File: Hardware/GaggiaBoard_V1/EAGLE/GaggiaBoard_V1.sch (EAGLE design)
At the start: 84 parts, among them IC1 LD117ADT33TR, J2 Vertical Qwiic Connector, J3 Vertical Qwiic Connector, J4 1X2-3.5MM, J5 1X2-3.5MM, K1 RELAY-SPDT-JZC-11F, K2 RELAY-SPDT-JZC-11F, K3 RELAY-SPDT-JZC-11F, Q1 600mA/40V, Q2 600mA/40V, Q3 600mA/40V, Q4 600mA/40V, Q5 600mA/40V, Q6 600mA/40V, Q7 2N7002D, Q8 600mA/40V, Q9 600mA/40V, U1 BLACKPILL, U2 MAX31855K, U3 MAX31855K, U4 MOC3021MDIL06O

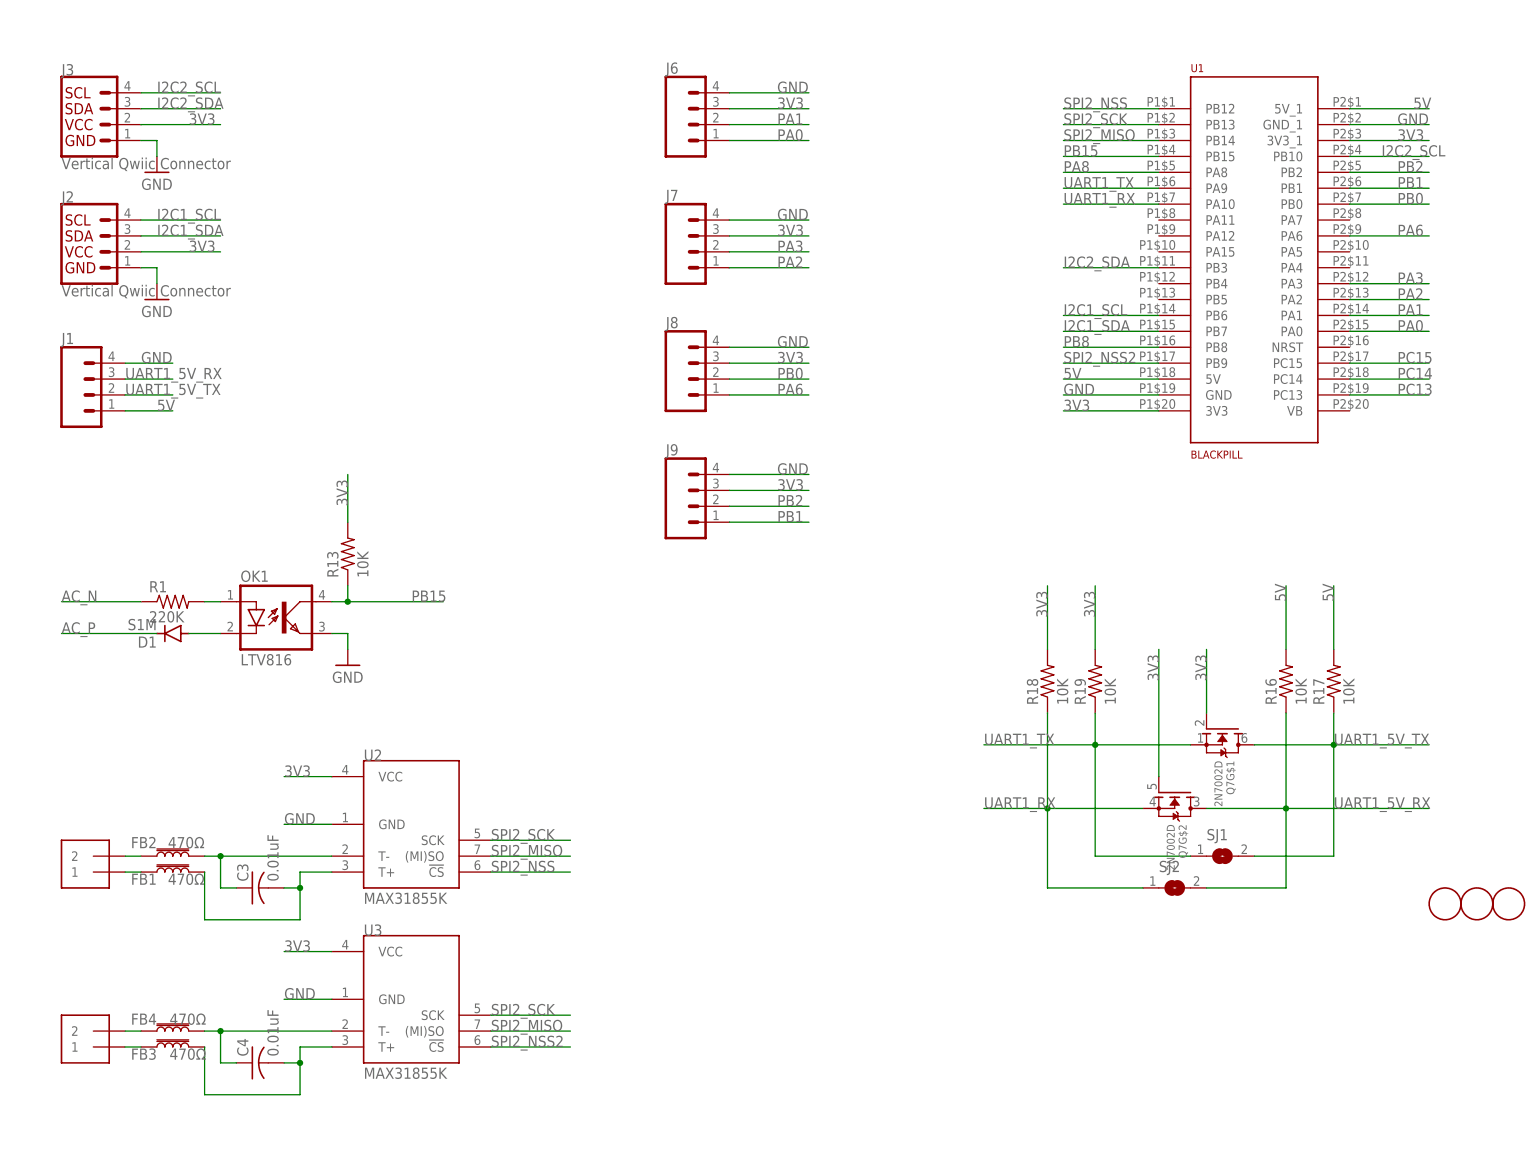
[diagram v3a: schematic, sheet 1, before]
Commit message: PSU replaced
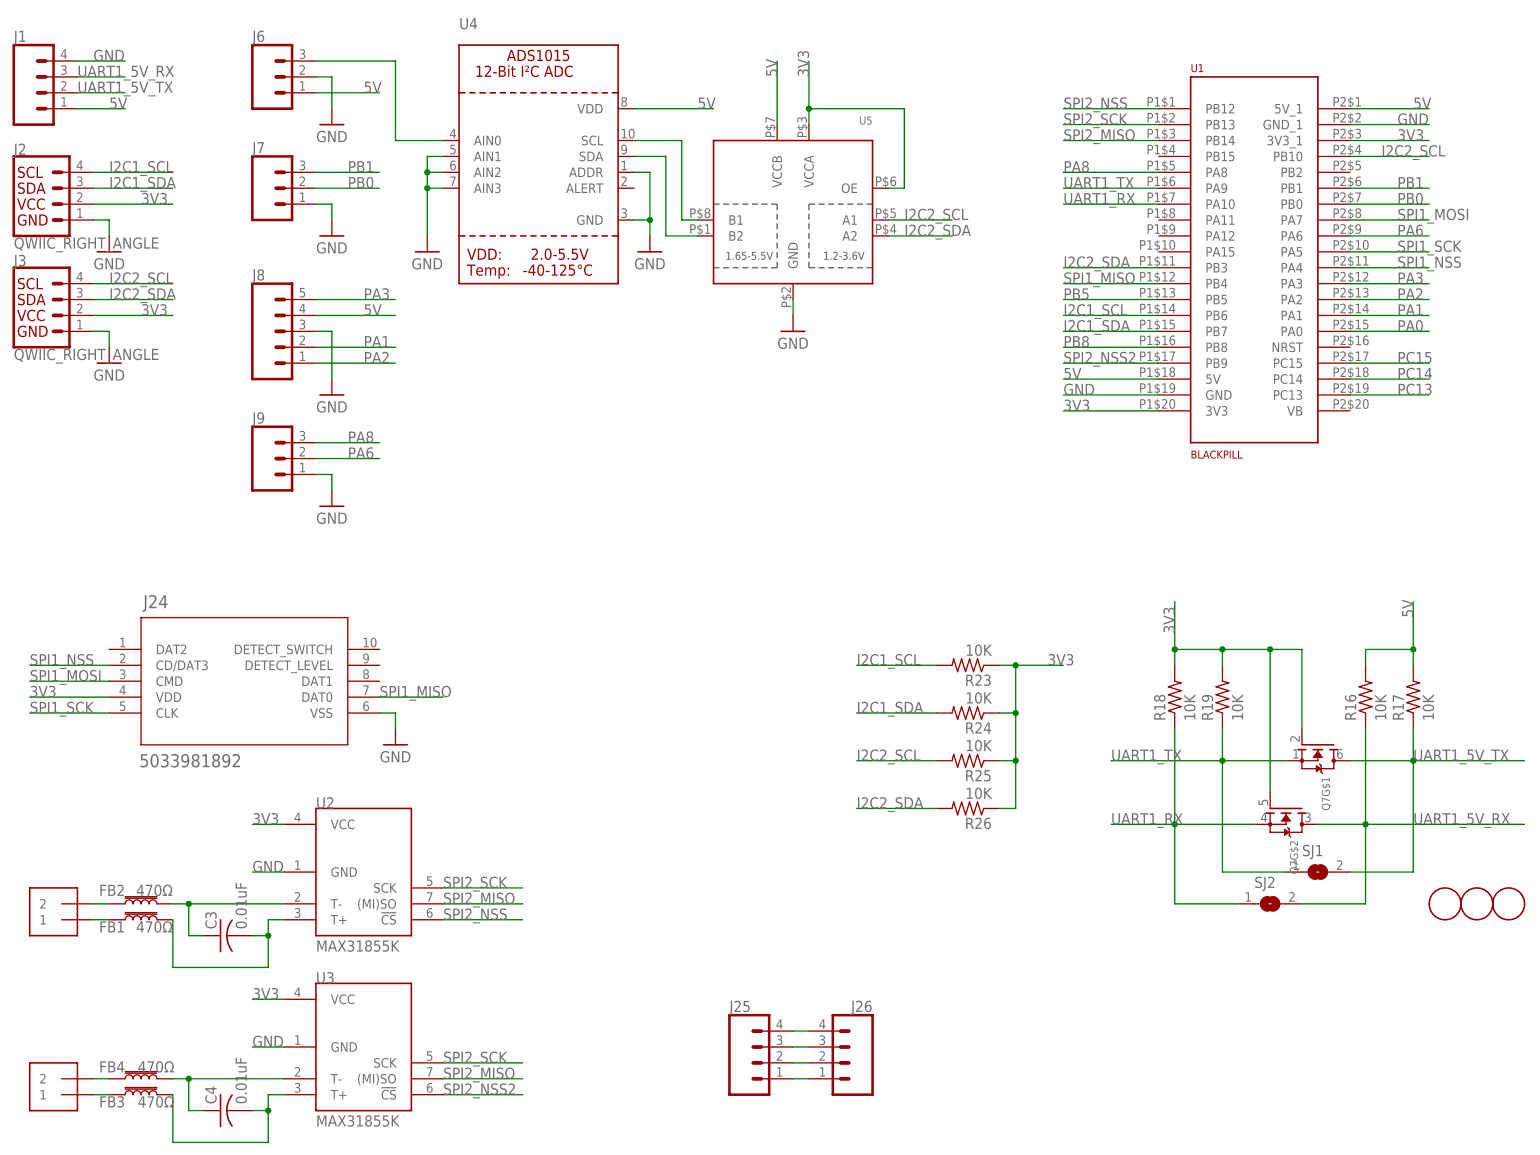
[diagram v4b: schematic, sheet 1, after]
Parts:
- removed PS1: PSK-3D-5, PSK-3D-5:PSK-3D-5
- removed X1, X2, X3, X4, X5, X6, X7: (no value), con-rib:SH5-2
- added B1: MB6S, rectifier:MB6S
- added B2: RECTIFIER-2KBP, rectifier:RECTIFIER-2KBP
- added C10, C11, C6, C7, C8, C9: 10uF/16V, rcl:C-USC0603
- added J10, J11, J12, J13, J14, J15, J16, J17, J18, J19, J20, J21, J22, J23: PIN262409-1, con-faston:PIN262409-1
- added J24: 5033981892, discrete:5033981892
- added J25, J26: (no value), SparkFun-Connectors:CONN_041X04_NO_SILK
- added OK2: MOC3021MDIL06O, discrete:MOC3021MDIL06O
- added PSU1: SM-PLG06-05, discrete:SM-PLG06-05
- added R22: 100, rcl:R-US_R0603
- added R23, R24, R25, R26: 10K, rcl:R-US_R0603
- added U5: (no value), adafruit:TXS0102
- C1, C2: device rcl:CPOL-USE2.5-5 -> rcl:C-USC0603; LCSC C19576 -> C86275
- C3, C4: device rcl:C-USC0805 -> rcl:C-USC0603; LCSC C2830723 -> C100042
- C5: LCSC C76989 -> C107192
- D1: value S1M -> 1N4007; device diode:S1M -> diode:DIODE-DO214AC; LCSC C155378 -> C727081
- F1: value 30A -> 6A; LCSC C3130 -> C206887
- FB1, FB2, FB3, FB4: LCSC C710387 -> C883591
- IC1: LCSC C165080 -> C152529
- J1: device SparkFun-Connectors:CONN_04PTH -> SparkFun-Connectors:CONN_04POLAR; LCSC C144395 -> C163037
- J2, J3: value Vertical Qwiic Connector -> QWIIC_RIGHT_ANGLE; device SparkFun-Connectors:QWIIC_CONNECTOR -> SparkFun-Connectors:QWIIC_CONNECTORJS-1MM; LCSC C160390 -> C160404
- J6, J7, J9: device SparkFun-Connectors:CONN_04JST-PTH-VERT -> SparkFun-Connectors:CONN_03JST-PTH; LCSC C131334 -> C157929
- J8: device SparkFun-Connectors:CONN_04JST-PTH-VERT -> SparkFun-Connectors:CONN_05JST; LCSC C131334 -> C157923
- LED1, LED2, LED3, LED4: LCSC C72042 -> C375534
- OK1: LCSC C115456 -> C2944043
- Q7: value 2N7002D -> (none); LCSC C383161 -> C150488
- R1: LCSC C2828895 -> C130275
- R10, R11, R12: value 330 -> 120; LCSC C351654 -> C114640
- R13, R16, R17, R18, R19, R20, R21: LCSC C328335 -> C98220
- R14: value 330 -> 51; LCSC C351654 -> C114628
- R15: LCSC C38808 -> C877859
- R2: device rcl:R-US_R1206 -> rcl:R-US_R0603; LCSC C95529 -> C114669
- R3, R4, R5, R6, R7, R8: device rcl:R-US_R0805 -> rcl:R-US_R0603; LCSC C328335 -> C98220
- R9: device rcl:R-US_R0805 -> rcl:R-US_R0603; LCSC C328441 -> C114669
- TR1: LCSC C145130 -> C71218
- U4: value MOC3021MDIL06O -> (none); device discrete:MOC3021MDIL06O -> microbuilder:ADC_ADS1015; LCSC C123202 -> C193969
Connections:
- removed net PB15: OK1.COL, R13.1, U1.PB15
- removed net PB2: J9.2, U1.PB2
- new net N$36: OK1.COL, R13.1, R22.1
- new net N$37: B1.AC2, R1.2
- new net N$38: U4.SDA, U5.B2
- new net N$39: OK2.A, R9.2
- new net N$40: B2.AC2, TR1.A1
- new net PB5: R20.1, U1.PB5
- new net PRESSURE: J6.3, U4.AIN0
- new net PUMP_N: B2.-, J21.1, R15.1
- new net SPI1_MISO: J24.DAT0, U1.PB4
- new net SPI1_MOSI: J24.CMD, U1.PA7
- new net SPI1_NSS: J24.CD/DAT3, U1.PA4
- new net SPI1_SCK: J24.CLK, U1.PA5
- new net SWCLK: J25.3, J26.3
- new net SWDIO: J25.2, J26.2
- net 3V3: now also C1.1, C2.1, C7.1, C8.1, C9.1, D1.C, J24.VDD, J25.1, J26.1, R23.1, R24.1, R25.1, R26.1, U5.OE, U5.VCCA; no longer C1.+, C2.+, J6.3, J7.3, J8.3, J9.3
- net 3WAY: now also J11.1; no longer X2-1.1, X2-1.2
- net 5V: now also C10.1, C11.1, J6.1, J8.4, PSU1.VO+, U4.VDD, U5.VCCB; no longer PS1.+VO
- net AC_N: now also B1.AC1, B2.AC1, J10.1, J12.1, J16.1, J22.1, PSU1.AC_N; no longer PS1.AC(N), R1.1, X1-2.1, X1-2.2, X2-2.1, X2-2.2, X3-2.1, X3-2.2, X4-2.1, X4-2.2, X5-2.1, X5-2.2
- net AC_P: now also J15.1, J19.1, K1.NC, K2.NC, K3.NC, OK2.A1, PSU1.AC_L, R1.1; no longer D1.C, PS1.AC(L), R15.1, U4.A1, X6-2.1, X6-2.2, X7-2.1, X7-2.2
- net GND: now also C1.2, C10.2, C11.2, C2.2, C6.2, C7.2, C8.2, C9.2, J24.VSS, J25.4, J26.4, J6.2, J7.1, J8.3, J9.1, OK2.C, PSU1.VO-, U4.ADDR, U4.AIN1, U4.AIN2, U4.AIN3, U4.GND, U5.GND; no longer C1.-, C2.-, J6.4, J7.4, J8.4, J9.4, PS1.-VO, R9.1
- net HEATER_1: now also J13.1, J14.1; no longer X3-1.1, X3-1.2, X6-1.1, X6-1.2
- net HEATER_2: now also J17.1, J18.1; no longer X4-1.1, X4-1.2, X7-1.1, X7-1.2
- net I2C1_SCL: now also R23.2
- net I2C1_SDA: now also R24.2
- net I2C2_SCL: now also R25.2, U5.A1
- net I2C2_SDA: now also R26.2, U5.A2
- net N$1: now also J23.1; no longer X1-1.1, X1-1.2
- net N$2: now also B1.+; no longer R1.2
- net N$22: now also U4.SCL, U5.B1; no longer R9.2, U4.C
- net N$30: now also D1.A
- net N$7: now also B1.-; no longer D1.A
- net N$8: now also OK2.A2; no longer U4.A2
- net PA0: now also C6.1, R22.2; no longer J6.1
- net PA1: now also J8.2; no longer J6.2
- net PA2: now also J8.1; no longer J7.1
- net PA3: now also J8.5; no longer J7.2
- net PA6: now also J9.2; no longer J8.1
- net PA8: now also J9.3; no longer R20.1
- net PB0: now also J7.2; no longer J8.2
- net PB1: now also J7.3; no longer J9.1
- net PB8: now also R9.1; no longer U4.A
- net PC13: now also R8.1; no longer R6.1
- net PC15: now also R6.1; no longer R8.1
- net PUMP_P: now also B2.+, J20.1; no longer TR1.A1, X5-1.1, X5-1.2
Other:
- moved on the sheet: C3, C4, C5, F1, FB1, FB2, FB3, FB4, IC1, J1, J2, J3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

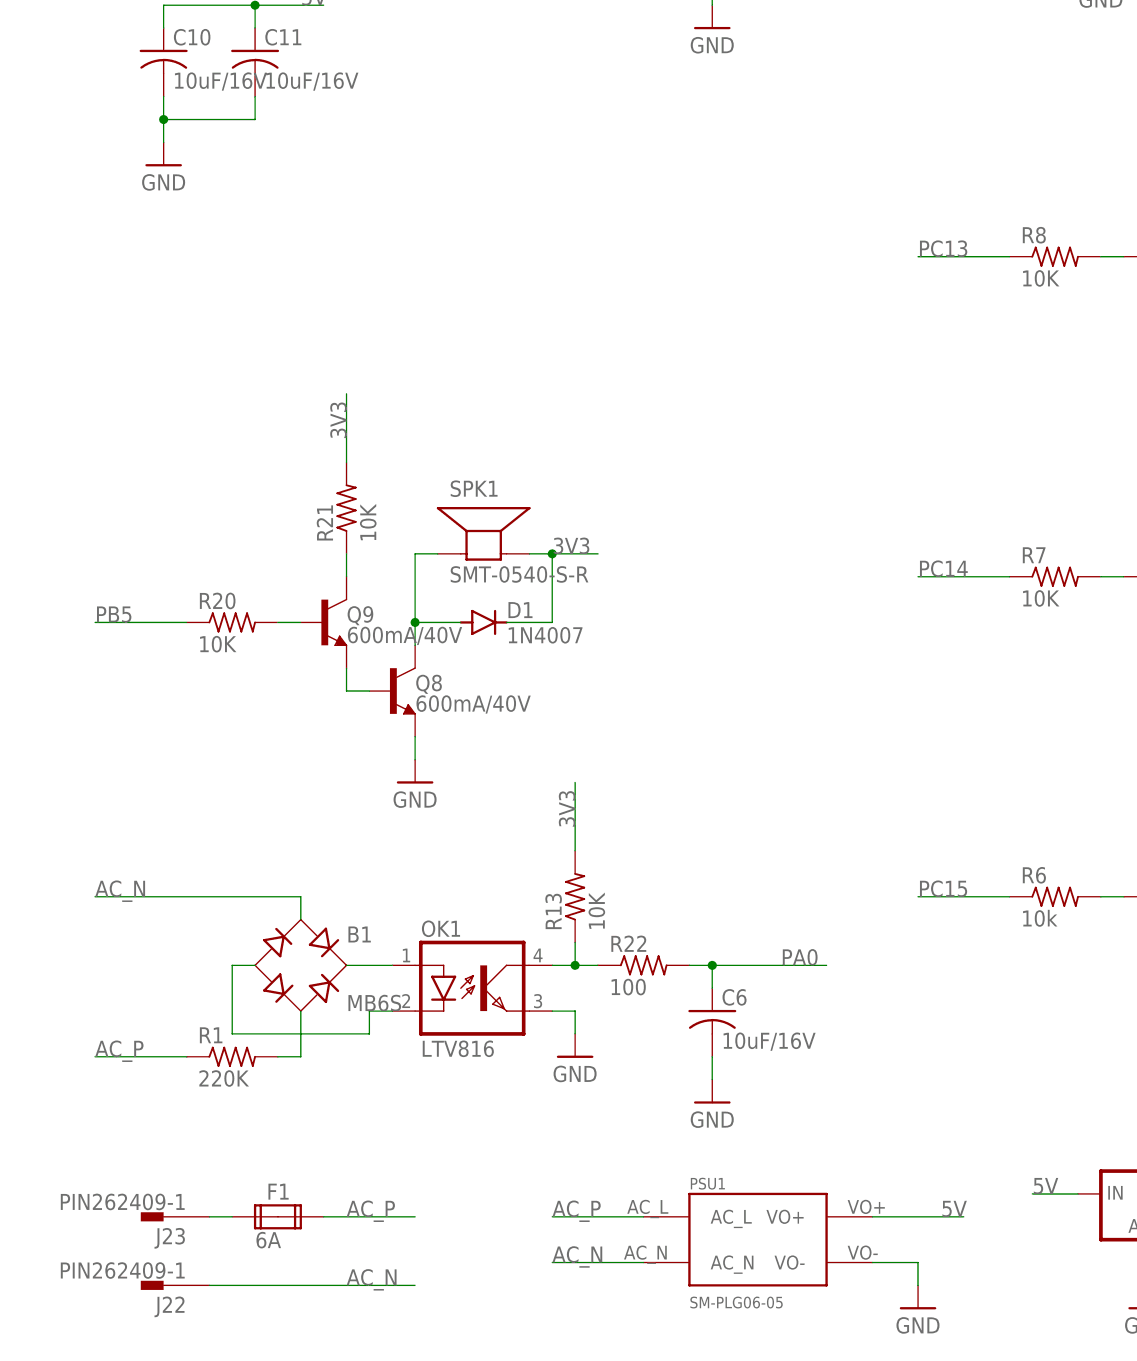
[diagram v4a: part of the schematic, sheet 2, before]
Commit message: MEAN WELL PSU option, discrete level shifters
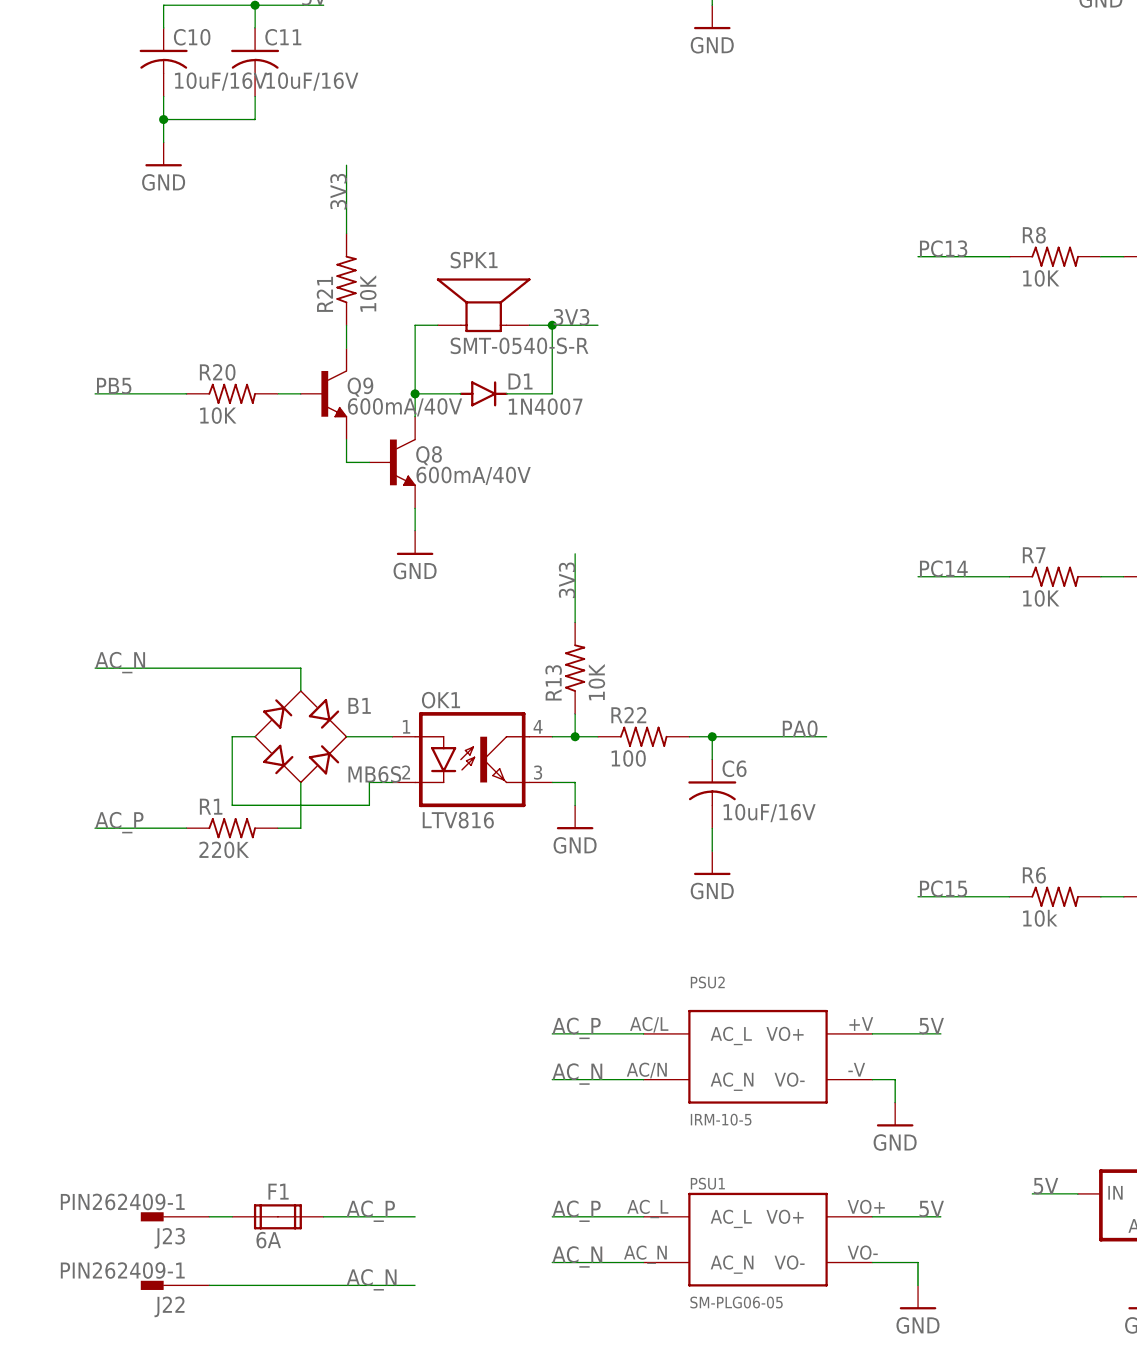
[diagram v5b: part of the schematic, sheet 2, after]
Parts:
- added PSU2: IRM-10-5, discrete:IRM-10-5
- added Q10, Q11, Q12: (no value), microbuilder:MOSFET-NREFLOW
- added R27, R28, R29, R30, R31, R32: 10K, rcl:R-US_R0603
- added SJ3, SJ4, SJ5: (no value), microbuilder:SOLDERJUMPER
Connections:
- new net N$41: J9.2, Q11.D, R30.2, SJ4.1
- new net N$42: J9.3, Q10.D, R29.2, SJ3.1
- new net N$43: J8.2, Q12.D, R32.1, SJ5.1
- net 3V3: now also Q10.G, Q11.G, Q12.G, R27.1, R28.1, R31.2
- net 5V: now also PSU2.VO+, R29.1, R30.1, R32.2
- net AC_N: now also PSU2.AC_N
- net AC_P: now also PSU2.AC_L
- net GND: now also PSU2.VO-
- net PA1: now also Q12.S, R31.1, SJ5.2; no longer J8.2
- net PA6: now also Q11.S, R28.2, SJ4.2; no longer J9.2
- net PA8: now also Q10.S, R27.2, SJ3.2; no longer J9.3
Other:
- moved on the sheet: B1, C6, D1, J24, J8, J9, OK1, Q8, Q9, R1, R13, R20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
